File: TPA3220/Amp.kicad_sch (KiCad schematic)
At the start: 7 parts, among them U1 TPA3220DDWR

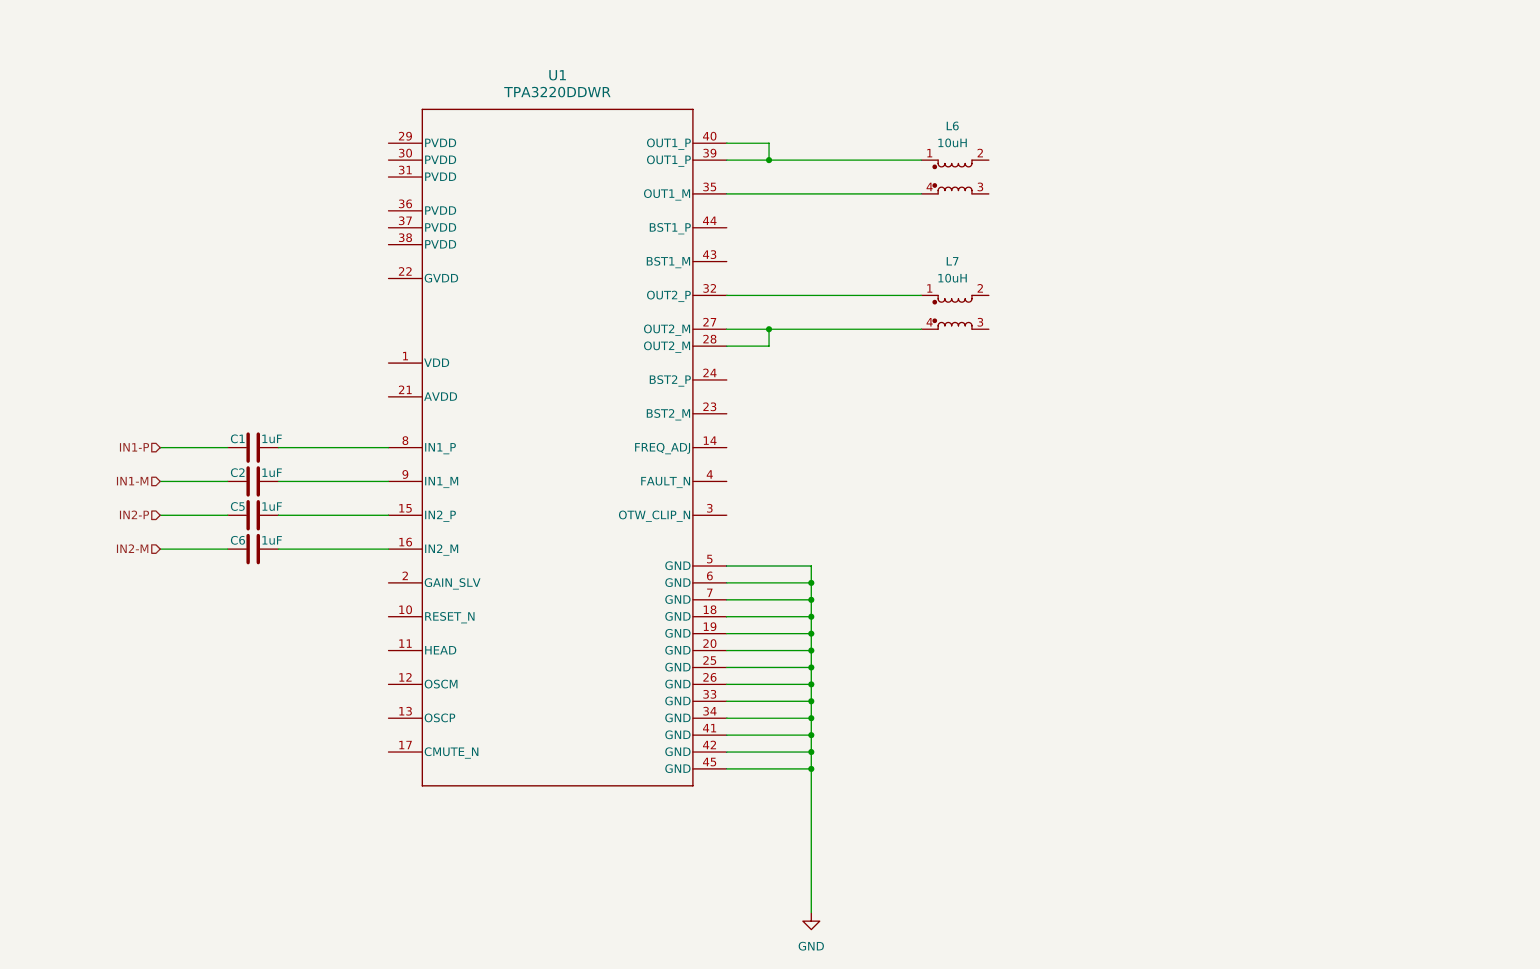
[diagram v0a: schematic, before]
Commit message: TPA3220: snapshot before agent schematic completion
Co-Authored-By: Claude Opus 5.5 <noreply@anthropic.com>
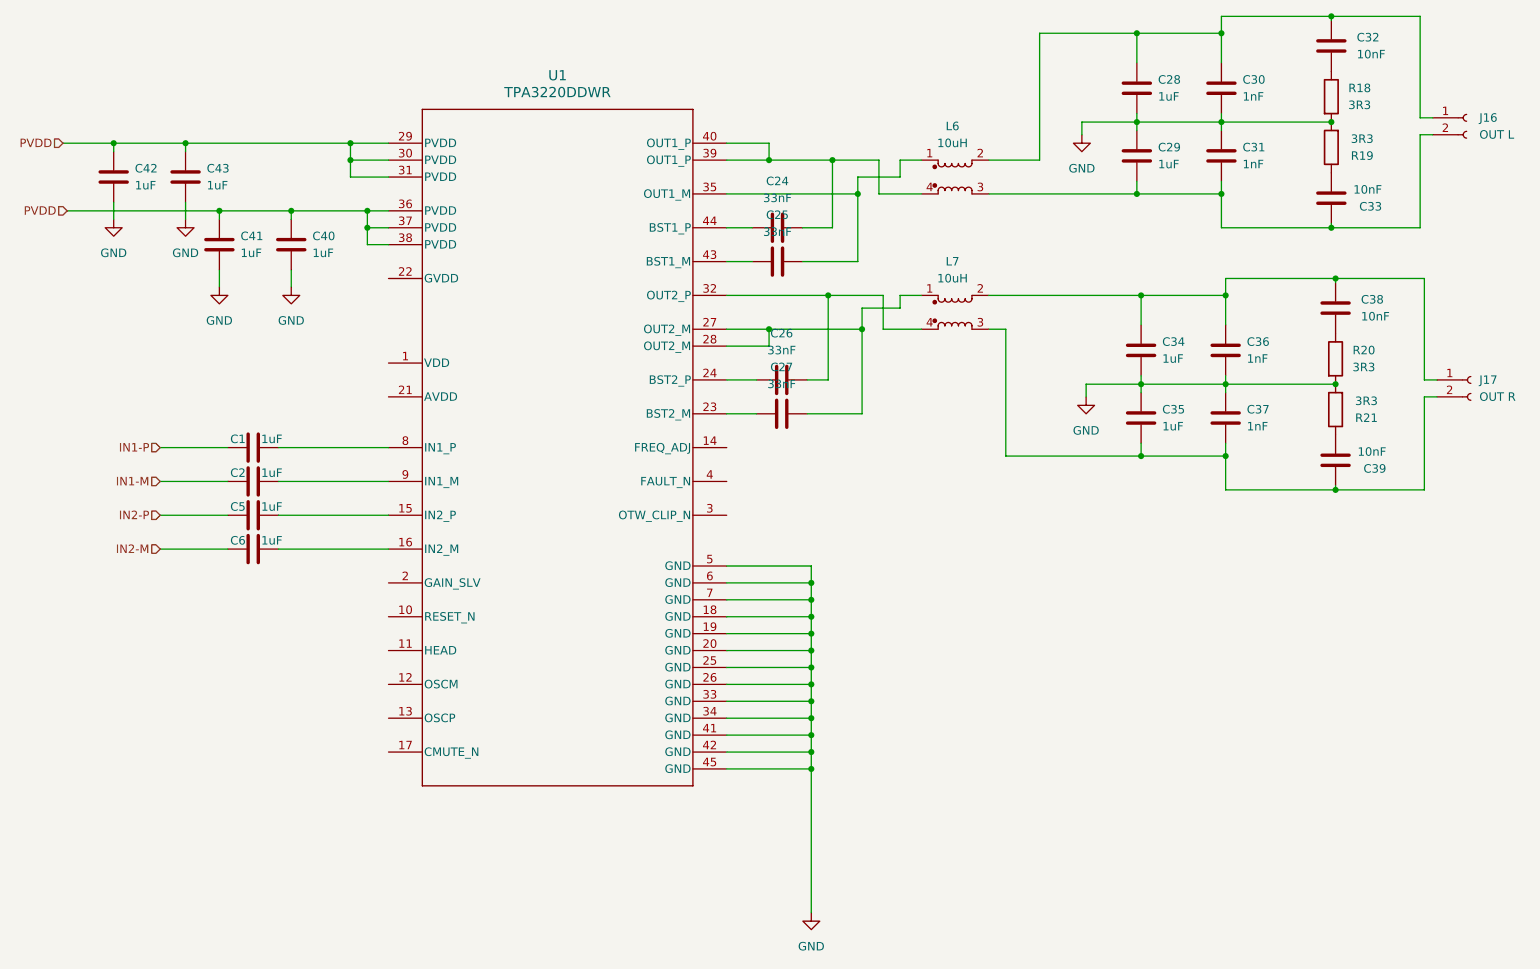
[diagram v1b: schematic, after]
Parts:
- added C24, C25, C26, C27: 33nF, Capacitor_SMD:C_0805_2012Metric_Pad1.18x1.45mm_HandSolder, symbol Device:C
- added C28, C29, C34, C35: 1uF, Capacitor_THT:C_Rect_L7.2mm_W5.5mm_P5.00mm_FKS2_FKP2_MKS2_MKP2, symbol Device:C
- added C30, C31, C36, C37: 1nF, Capacitor_SMD:C_0805_2012Metric_Pad1.18x1.45mm_HandSolder, symbol Device:C
- added C32, C33, C38, C39: 10nF, Capacitor_SMD:C_0805_2012Metric_Pad1.18x1.45mm_HandSolder, symbol Device:C
- added C40, C41, C42, C43: 1uF, Capacitor_SMD:C_1206_3216Metric_Pad1.33x1.80mm_HandSolder, symbol Device:C
- added J16: OUT L, Connector_Molex:Molex_KK-396_A-41791-0002_1x02_P3.96mm_Vertical, symbol Connector:Conn_01x02_Socket
- added J17: OUT R, Connector_Molex:Molex_KK-396_A-41791-0002_1x02_P3.96mm_Vertical, symbol Connector:Conn_01x02_Socket
- added R18, R19, R20, R21: 3R3, Resistor_SMD:R_2512_6332Metric_Pad1.40x3.35mm_HandSolder, symbol Device:R
- U1: footprint Custom:TPA3220 -> TPA3220:TPA3220_DDW0044D_HTSSOP-44_6.1x14mm_P0.635mm_EP5.2x14mm_Mask4.43x7.3mm_ThermalVias
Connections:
- net GND: now also C28.2, C29.1, C30.1, C31.2, C34.2, C35.1, C36.1, C37.2, C40.2, C41.2, C42.2, C43.2, R18.2, R19.2, R20.2, R21.2
- net at U1.39 (OUT1_P), U1.40 (OUT1_P): now also L6.4, C24.2; no longer L6.1
- net at L6.2: now also C28.1, C30.2, C32.2, J16.1 (Pin_1)
- net at L6.3: now also C29.2, C31.1, C33.2, J16.2 (Pin_2)
- net at U1.35 (OUT1_M): now also L6.1, C25.2; no longer L6.4
- net at U1.23 (BST2_M): now also C27.1
- net at U1.24 (BST2_P): now also C26.1
- net at U1.27 (OUT2_M), U1.28 (OUT2_M): now also L7.1, C27.2; no longer L7.4
- net PVDD: now reaches U1.29 (PVDD)
- net PVDD: now also U1.30 (PVDD), U1.31 (PVDD), U1.36 (PVDD), U1.37 (PVDD), U1.38 (PVDD), C40.1, C41.1, C42.1, C43.1
- net at U1.32 (OUT2_P): now also L7.4, C26.2; no longer L7.1
- net at U1.43 (BST1_M): now also C25.1
- net at U1.44 (BST1_P): now also C24.1
- net at L7.2: now also C34.1, C36.2, C38.2, J17.1 (Pin_1)
- net at L7.3: now also C35.2, C37.1, C39.2, J17.2 (Pin_2)
- new net: C32.1, R18.1
- new net: C38.1, R20.1
- new net: C39.1, R21.1
- new net: C33.1, R19.1
